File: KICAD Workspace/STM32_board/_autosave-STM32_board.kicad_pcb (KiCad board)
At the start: 2 copper layers, 171.4 x 151.8 mm, 26 parts, among them J1 Power connector, J10 Low side connector, J2 High side connector, J3 Sensors connector, J4 LCD interface, J5 Low side connector, J6 3v3_out, J7 Joystick connector, J8 External Pins, J9 UART module, U1 CD4050BE, U2 LM7805_TO220, U3 LP2950-3.3_TO92

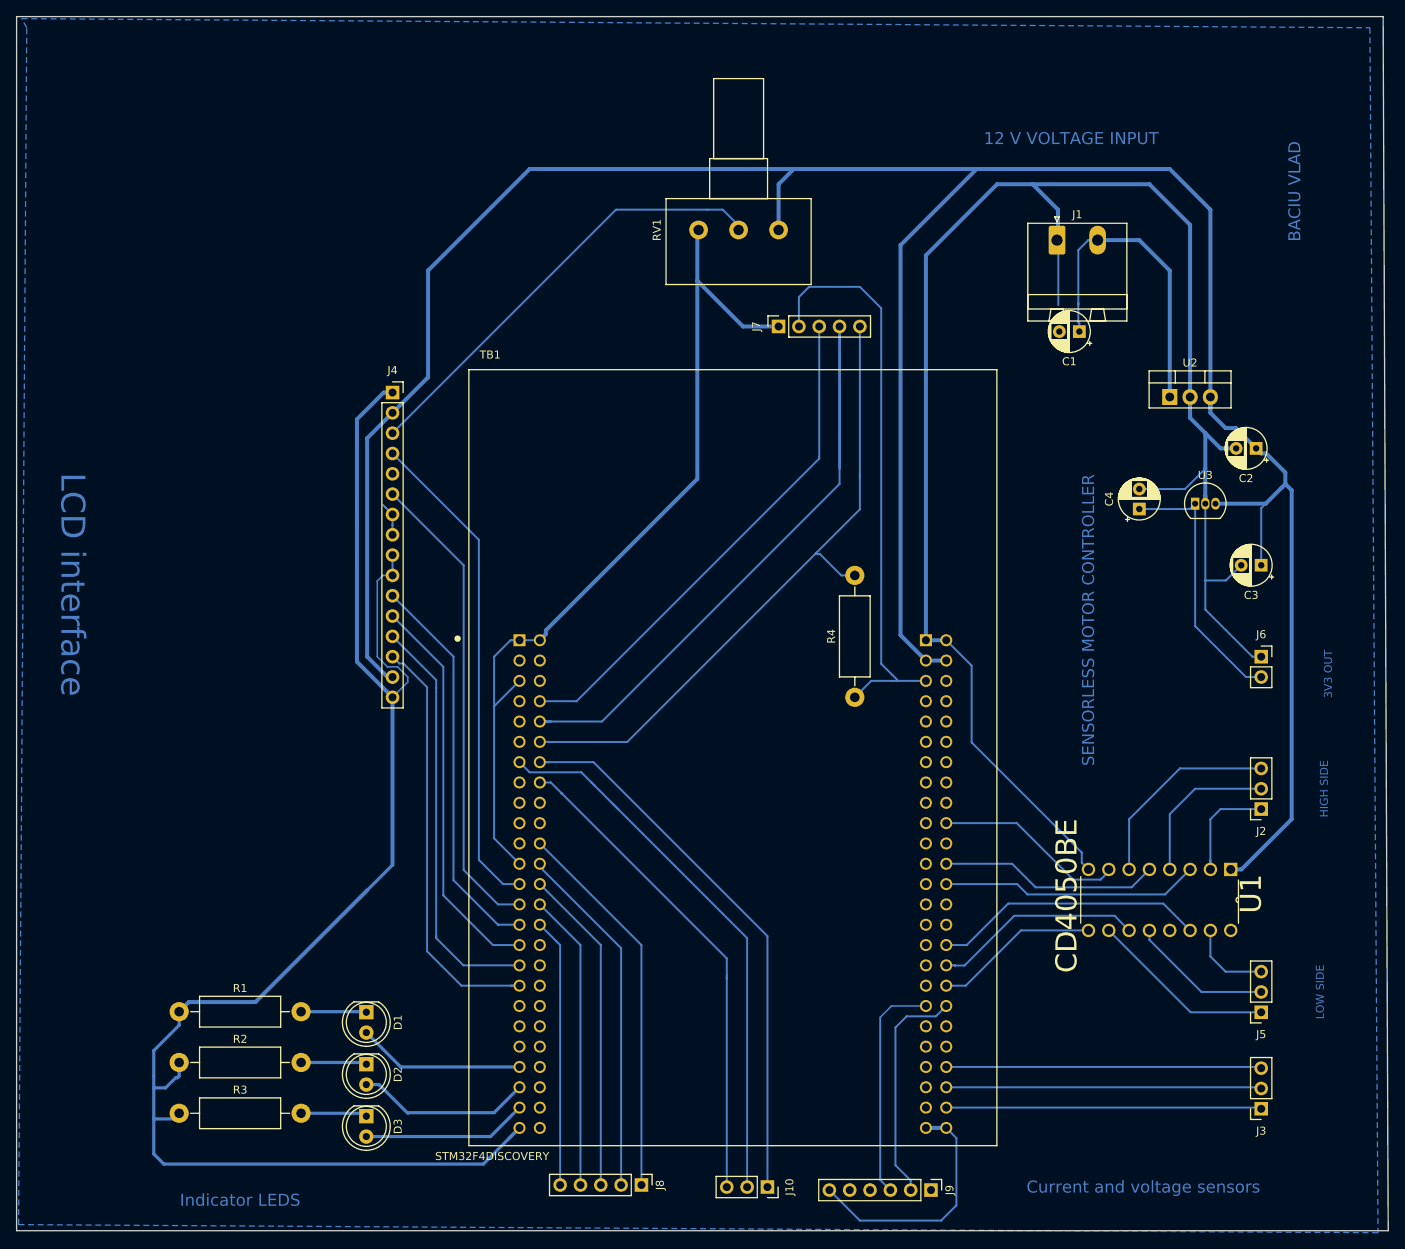
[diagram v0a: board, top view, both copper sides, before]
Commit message: Modifications of layout. Added some connectors, deleted others, pins connections changed
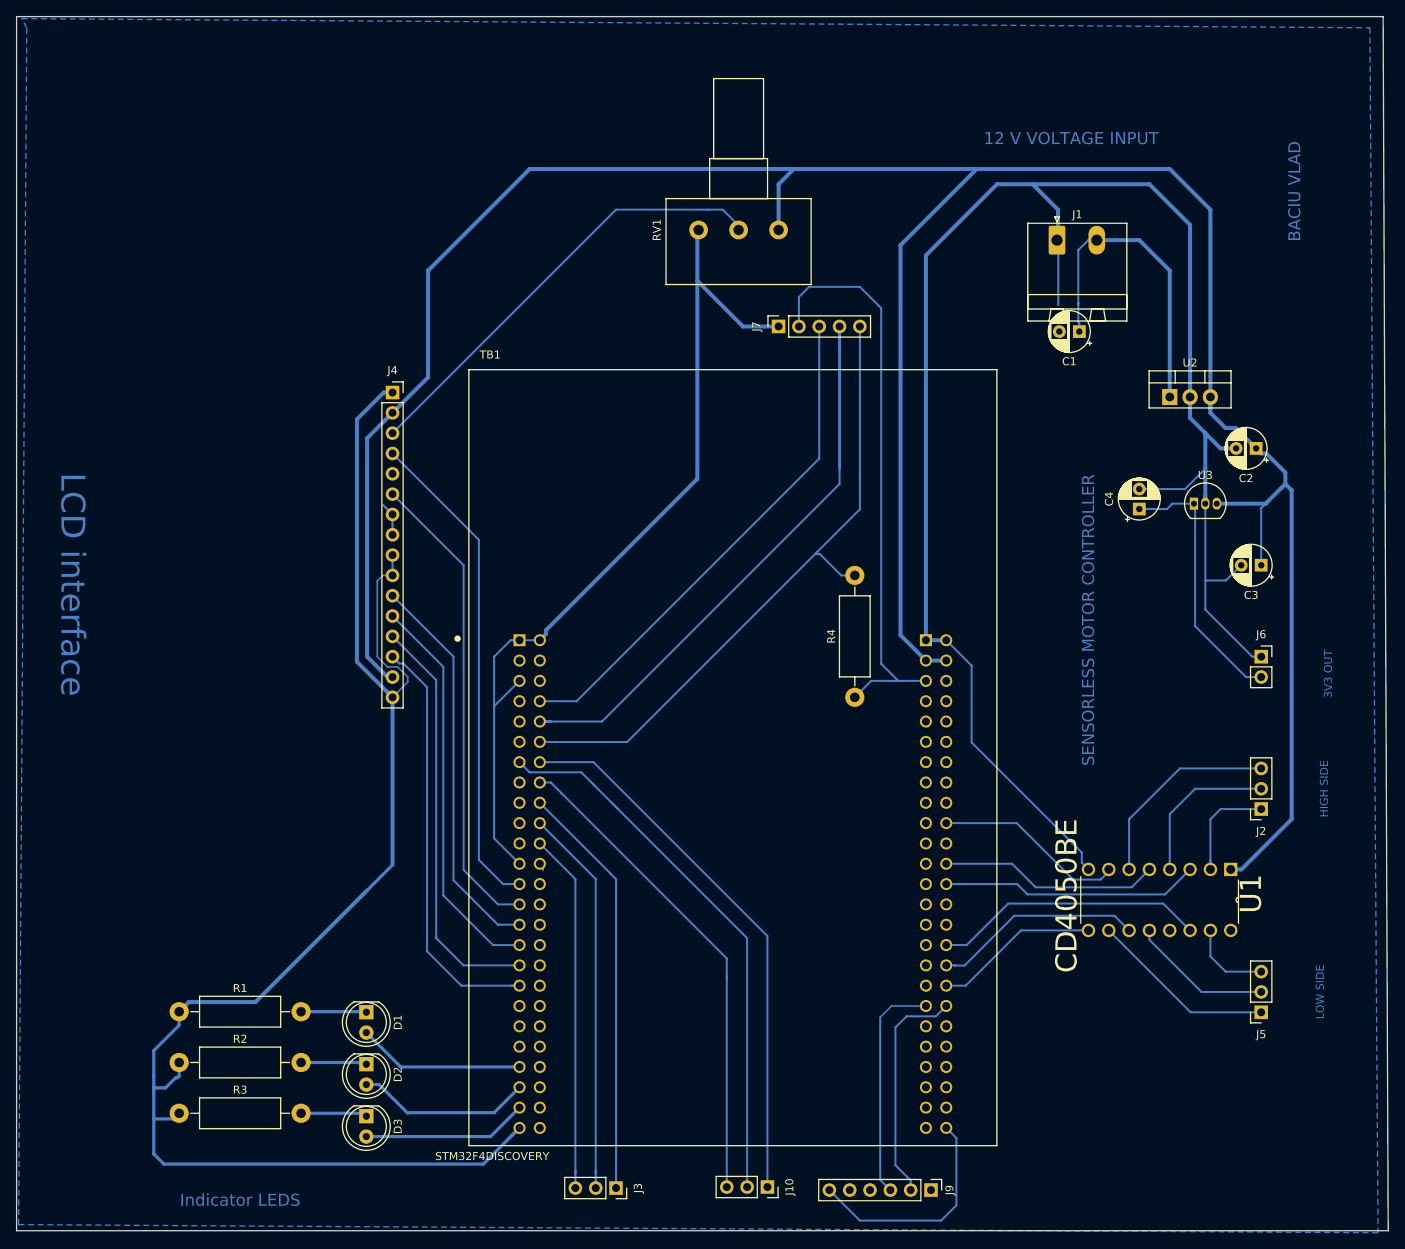
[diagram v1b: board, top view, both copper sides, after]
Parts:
- removed J8: External Pins, Connector_PinHeader_2.54mm:PinHeader_1x05_P2.54mm_Vertical
- moved J3 81.3 mm to (92.3, 160.4), turned to 270 degrees
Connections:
- J3 pad 1: /ADC_BATTERY -> /CURRENT_SENSOR
- J3 pad 2: /CURRENT_SENSOR -> /ADC_BATTERY
- TB1 pad P1_18: Net-(TB1-PadP1_18) -> /CURRENT_SENSOR
- TB1 pad P1_20: Net-(TB1-PadP1_20) -> /ADC_BATTERY
- TB1 pad P1_22: /EXT_3 -> /READ_BATTERY
- TB1 pad P2_44: /READ_BATTERY -> Net-(TB1-PadP2_44)
- TB1 pad P2_46: /CURRENT_SENSOR -> Net-(TB1-PadP2_46)
- TB1 pad P2_48: /ADC_BATTERY -> Net-(TB1-PadP2_48)
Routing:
- net /EXT_3: track 48.6 -> 0.00 mm
- net /EXT_4: track 45.4 -> 1.34 mm
- net /EXT_5: track 41.4 -> 0.00 mm
- net /EXT_6: track 37.8 -> 0.00 mm
- net /EXT_7: track 34.2 -> 0.00 mm
- net /CURRENT_SENSOR: track 39.4 -> 53.4 mm
- net /ADC_BATTERY: track 39.4 -> 49.1 mm
- net /READ_BATTERY: track 39.4 -> 45.3 mm
- net /GND: track 606.2 -> 603.7 mm
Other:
- board text removed: "Current and voltage sensors"
